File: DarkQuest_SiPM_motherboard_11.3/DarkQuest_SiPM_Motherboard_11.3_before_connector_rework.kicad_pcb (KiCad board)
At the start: 2 copper layers, 100 x 100 mm, 18 parts, among them J17 SiPM Chip Pin Header (K), J18 SiPM Chip Pin Header (K), J19 SiPM Chip Pin Header (K), J20 SiPM Chip Pin Header (K), J21 RJ45_Shielded, J5 SiPM Chip Pin Header (A), J6 SiPM Chip Pin Header (A), J7 SiPM Chip Pin Header (A), J8 SiPM Chip Pin Header (A)

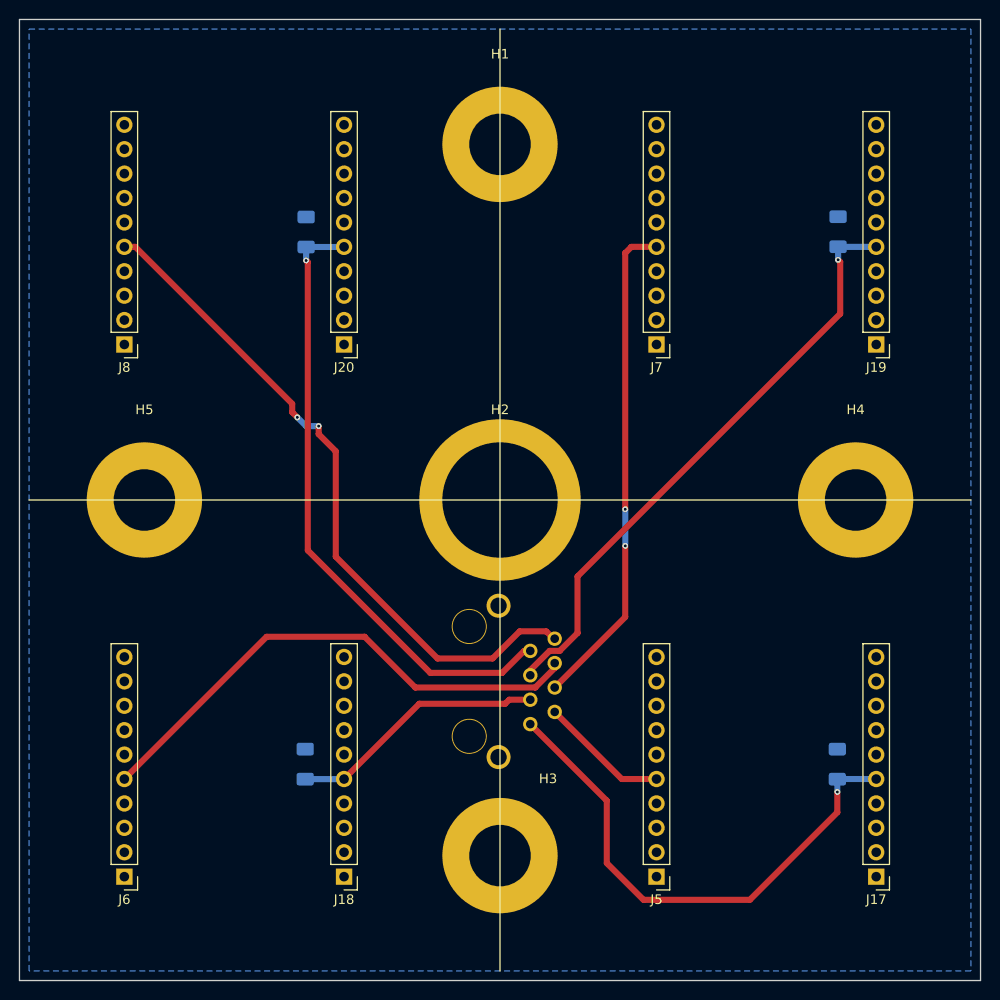
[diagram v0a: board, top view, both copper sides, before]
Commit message: slight rework to simplify routing around the RJ-45 connector. Added version with 4 layers and 50 ohm lines in case its needed
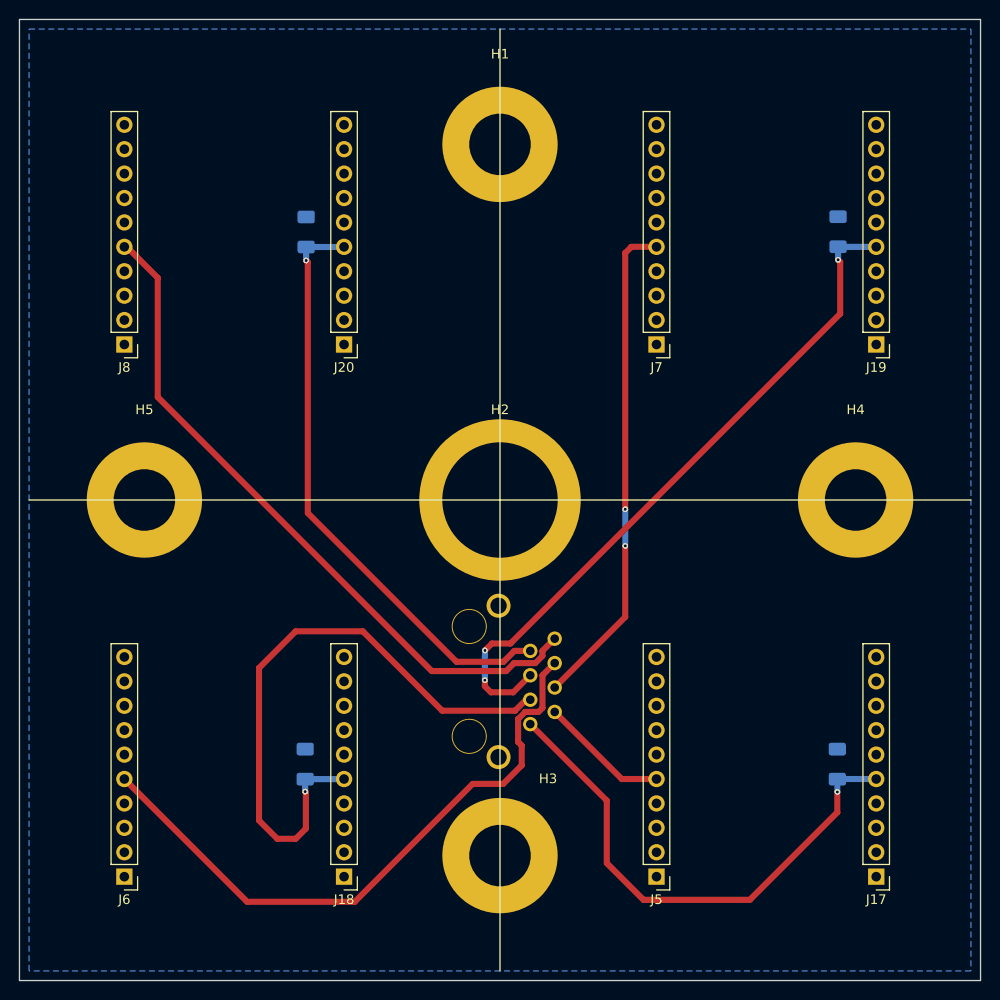
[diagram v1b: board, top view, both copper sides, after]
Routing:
- net /K1: track 26.8 -> 64.9 mm, vias 0 -> 1
- net /A1: track 54.5 -> 65.7 mm
- net /K2: track 62.6 -> 72.0 mm, vias 1 -> 3
- net /K3: track 65.0 -> 61.7 mm
- net /A3: track 71.6 -> 72.0 mm, vias 2 -> 0
